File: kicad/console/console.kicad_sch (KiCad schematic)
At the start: 4 parts, among them SW1 SW_DPST_x2

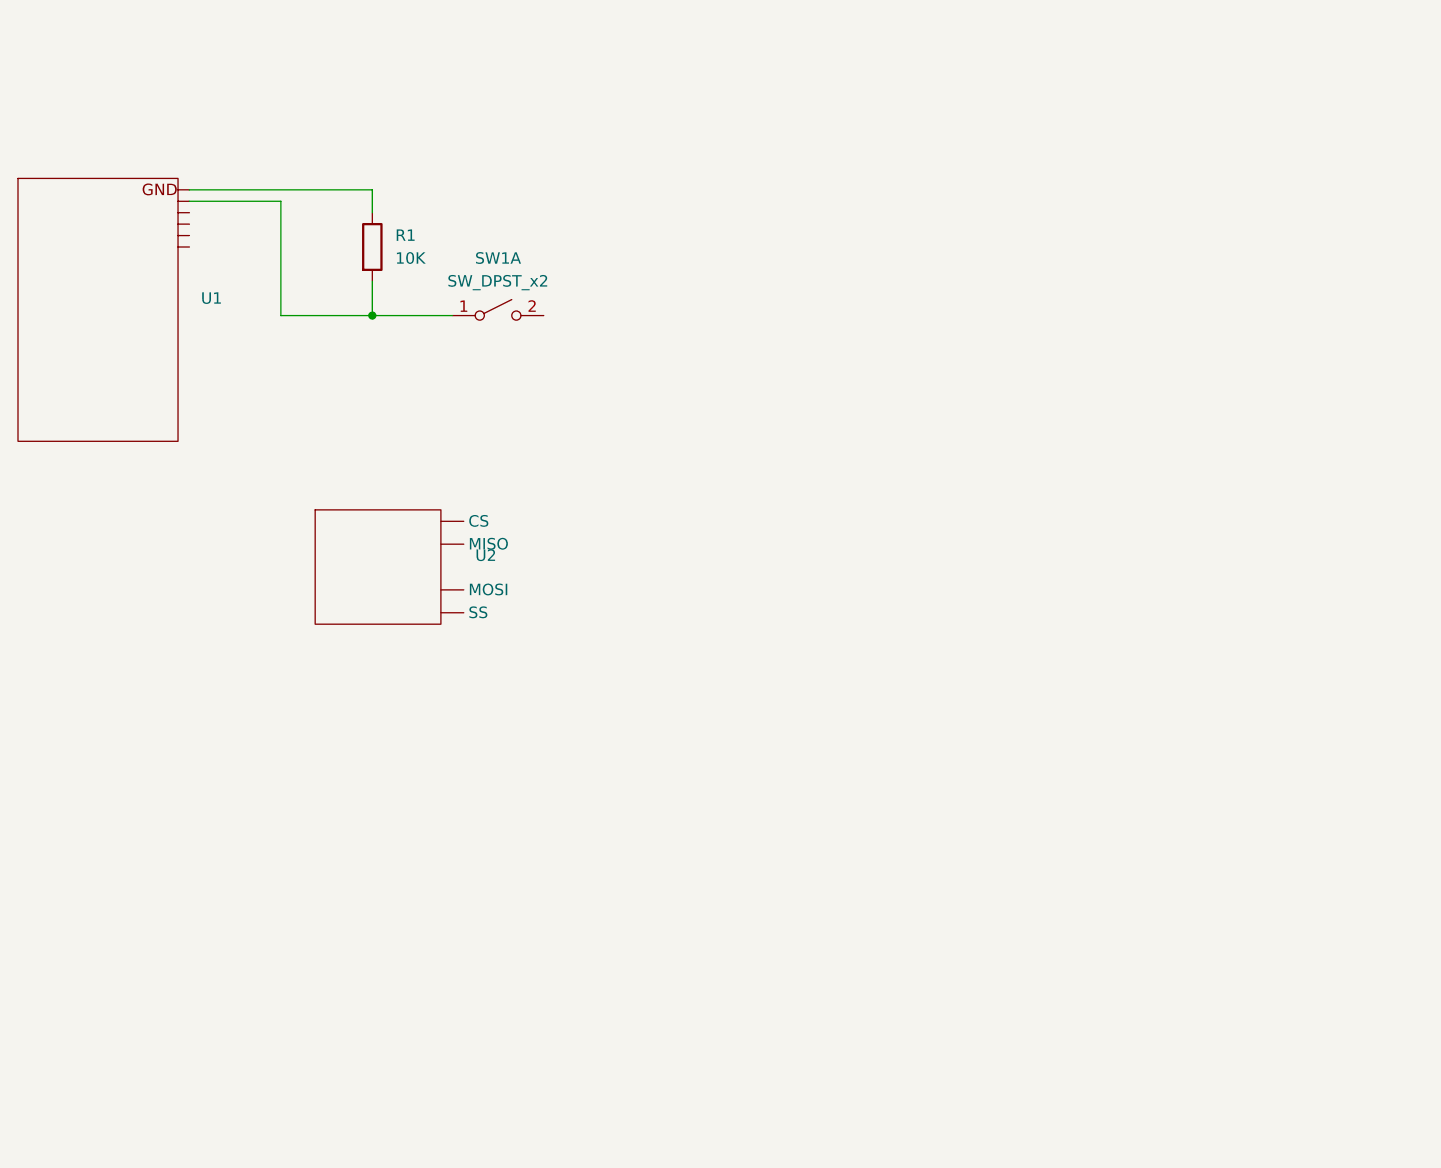
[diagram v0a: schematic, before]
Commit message: kicad schaltplan aktualisiert. es gibt nun eine footprint bibliothek und eine symbolbibliothek.
symbole findet man in der symbols library "console_library" und footprints in der footprint library "console_footprints"
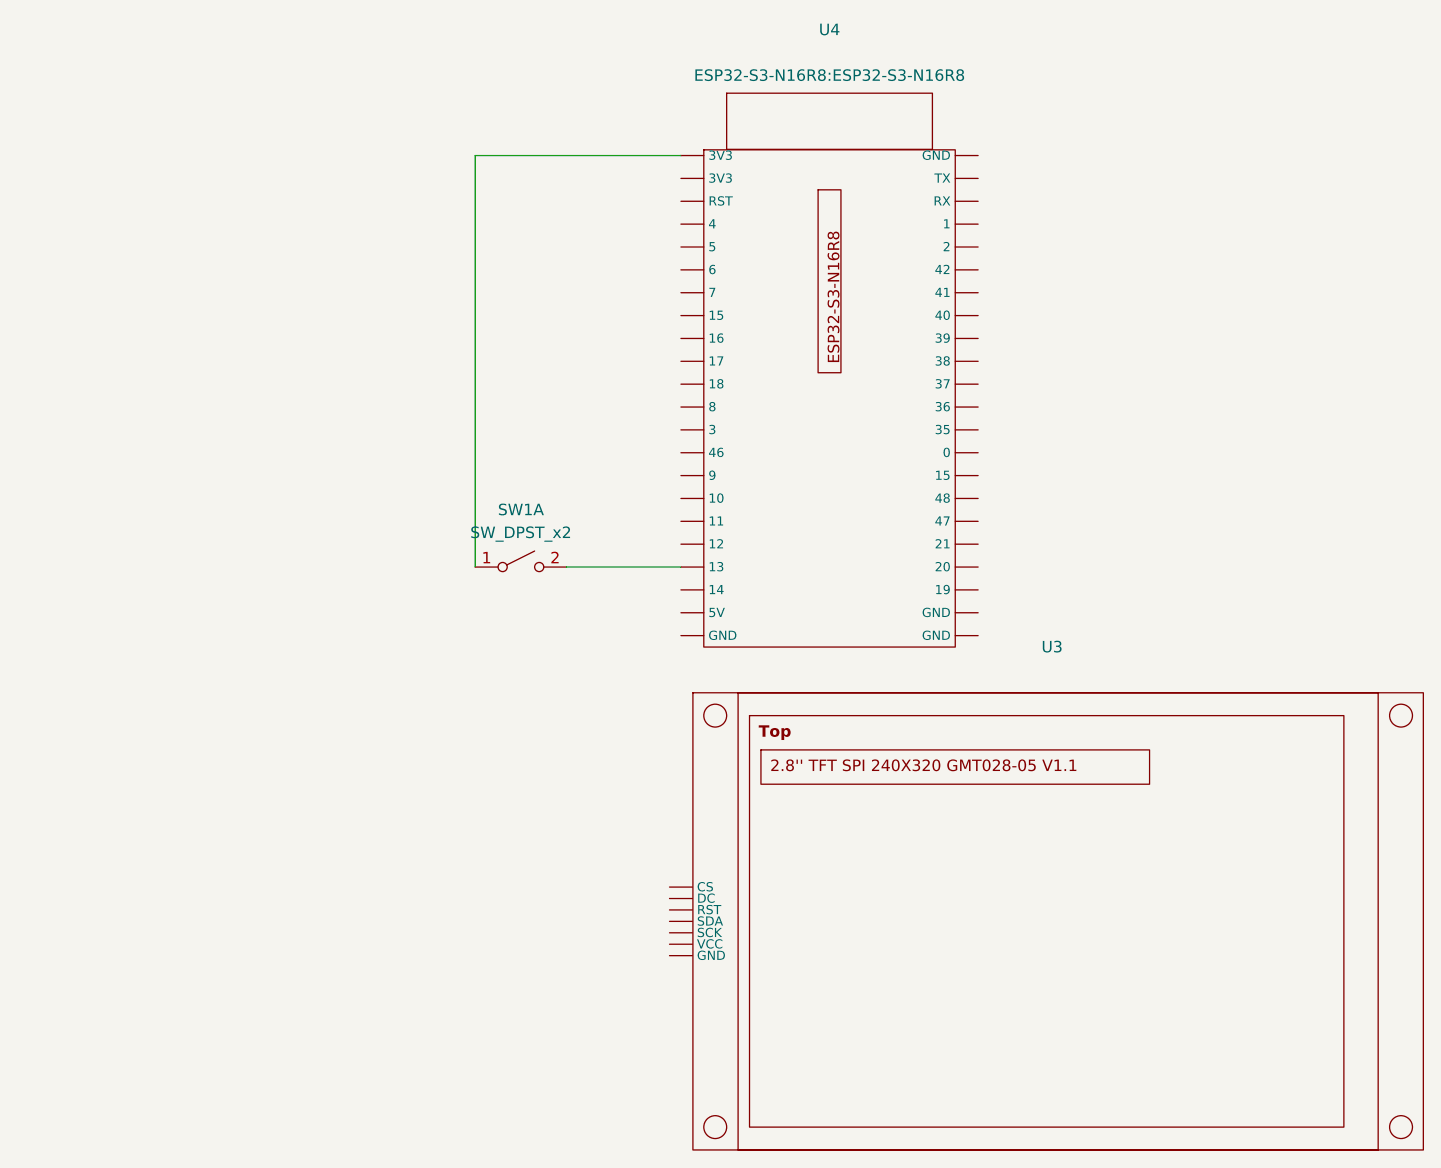
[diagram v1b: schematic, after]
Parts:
- removed R1: 10K, symbol Device:R
- removed U1: ~, symbol console_library:ESP32-S3-N16R8_1
- removed U2: ~, symbol console_library:SPI
- added U3: ~, console_footprints:2.8''_TFT_SPI_240X320_GMT028-05_V1.1, symbol console_library:2.8''_TFT_SPI_240X320_GMT028-05_V1.1
- added U4: ~, ESP32-S3-N16R8:ESP32-S3-N16R8, symbol console_library:ESP32-S3-N16R8
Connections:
- net at SW1.1 (A): now also U4. (GND)
- net at SW1.2 (B): now also U4. (GND)
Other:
- moved on the sheet: SW1A
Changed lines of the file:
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@@
 	(generator_version "9.0")
 	(paper "A4")
-	(junction
-		(at 115.57 68.58)
-		(diameter 0)
-		(color 0 0 0 0)
-	)
 	(wire
 		(pts
-			(xy 115.57 68.58) (xy 124.46 68.58)
+			(xy 137.16 96.52) (xy 149.86 96.52)
 		)
 		(stroke
@@
 	(wire
 		(pts
-			(xy 105.41 55.88) (xy 105.41 68.58)
+			(xy 127 50.8) (xy 149.86 50.8)
 		)
 		(stroke
@@
 	(wire
 		(pts
-			(xy 115.57 57.15) (xy 115.57 54.61)
+			(xy 127 96.52) (xy 127 50.8)
 		)
 		(stroke
@@
 		)
 	)
-	(wire
-		(pts
-			(xy 95.25 54.61) (xy 115.57 54.61)
-		)
-		(stroke
-			(width 0)
-			(type default)
-		)
-	)
-	(wire
-		(pts
-			(xy 115.57 68.58) (xy 105.41 68.58)
-		)
-		(stroke
-			(width 0)
-			(type default)
-		)
-	)
-	(wire
-		(pts
-			(xy 115.57 64.77) (xy 115.57 68.58)
-		)
-		(stroke
-			(width 0)
-			(type default)
-		)
-	)
-	(wire
-		(pts
-			(xy 95.25 55.88) (xy 105.41 55.88)
-		)
-		(stroke
-			(width 0)
-			(type default)
-		)
-	)
 	(symbol
 		(lib_id "Switch:SW_DPST_x2")
-		(at 129.54 68.58 0)
+		(at 132.08 96.52 0)
 		(unit 1)
 		(exclude_from_sim no)
@@
 		(fields_autoplaced yes)
 		(property "Reference" "SW1"
-			(at 129.54 62.23 0)
+			(at 132.08 90.17 0)
 			(effects
 				(font
@@
 		)
 		(property "Value" "SW_DPST_x2"
-			(at 129.54 64.77 0)
+			(at 132.08 92.71 0)
 			(effects
 				(font
@@
 		)
 		(property "Footprint" ""
-			(at 129.54 68.58 0)
+			(at 132.08 96.52 0)
 			(effects
 				(font
@@
 		)
 		(property "Datasheet" "~"
-			(at 129.54 68.58 0)
+			(at 132.08 96.52 0)
 			(effects
 				(font
@@
 		)
 		(property "Description" "Single Pole Single Throw (SPST) switch, separate symbol"
-			(at 129.54 68.58 0)
+			(at 132.08 96.52 0)
 			(effects
 				(font
@@
 	)
 	(symbol
-		(lib_id "Device:R")
-		(at 115.57 60.96 0)
+		(lib_id "console_library:ESP32-S3-N16R8")
+		(at 166.37 78.74 0)
 		(unit 1)
 		(exclude_from_sim no)
@@
 		(dnp no)
 		(fields_autoplaced yes)
-		(property "Reference" "R1"
-			(at 118.11 59.6899 0)
-			(effects
-				(font
-					(size 1.27 1.27)
-				)
-				(justify left)
-			)
-		)
-		(property "Value" "10K"
-			(at 118.11 62.2299 0)
-			(effects
-				(font
-					(size 1.27 1.27)
-				)
-				(justify left)
-			)
-		)
-		(property "Footprint" ""
-			(at 113.792 60.96 90)
-			(effects
-				(font
-					(size 1.27 1.27)
-				)
-				(hide yes)
-			)
-		)
-		(property "Datasheet" "~"
-			(at 115.57 60.96 0)
-			(effects
-				(font
-					(size 1.27 1.27)
-				)
-				(hide yes)
-			)
-		)
-		(property "Description" "Resistor"
-			(at 115.57 60.96 0)
-			(effects
-				(font
-					(size 1.27 1.27)
-				)
-				(hide yes)
-			)
-		)
-		(pin "1"
-		)
-		(pin "2"
+		(property "Reference" "U4"
+			(at 166.37 36.83 0)
+			(effects
+				(font
+					(size 1.27 1.27)
+				)
+			)
+		)
+		(property "Value" "~"
+			(at 166.37 39.37 0)
+			(effects
+				(font
+					(size 1.27 1.27)
+				)
+			)
+		)
+		(property "Footprint" "ESP32-S3-N16R8:ESP32-S3-N16R8"
+			(at 166.37 41.91 0)
+			(effects
+				(font
+					(size 1.27 1.27)
+				)
+			)
+		)
+		(property "Datasheet" ""
+			(at 166.37 78.74 0)
+			(effects
+				(font
+					(size 1.27 1.27)
+				)
+				(hide yes)
+			)
+		)
+		(property "Description" ""
+			(at 166.37 78.74 0)
+			(effects
+				(font
+					(size 1.27 1.27)
+				)
+				(hide yes)
+			)
+		)
+		(pin ""
+		)
+		(pin ""
+		)
+		(pin ""
+		)
+		(pin ""
+		)
+		(pin ""
+		)
+		(pin ""
+		)
+		(pin ""
+		)
+		(pin ""
+		)
+		(pin ""
+		)
+		(pin ""
+		)
+		(pin ""
+		)
+		(pin ""
+		)
+		(pin ""
+		)
+		(pin ""
+		)
+		(pin ""
+		)
+		(pin ""
+		)
+		(pin ""
+		)
+		(pin ""
+		)
+		(pin ""
+		)
+		(pin ""
+		)
+		(pin ""
+		)
+		(pin ""
+		)
+		(pin ""
+		)
+		(pin ""
+		)
+		(pin ""
+		)
+		(pin ""
+		)
+		(pin ""
+		)
+		(pin ""
+		)
+		(pin ""
+		)
+		(pin ""
+		)
+		(pin ""
+		)
+		(pin ""
+		)
+		(pin ""
+		)
+		(pin ""
+		)
+		(pin ""
+		)
+		(pin ""
+		)
+		(pin ""
+		)
+		(pin ""
+		)
+		(pin ""
+		)
+		(pin ""
+		)
+		(pin ""
+		)
+		(pin ""
+		)
+		(pin ""
+		)
+		(pin ""
 		)
 		(instances
 			(project ""
 				(path "/62a2f419-179e-43b6-8483-7e1508ae9f10"
-					(reference "R1")
+					(reference "U4")
 					(unit 1)
 				)
@@
 	)
 	(symbol
-		(lib_id "console_library:SPI")
-		(at 115.57 95.25 0)
+		(lib_id "console_library:2.8''_TFT_SPI_240X320_GMT028-05_V1.1")
+		(at 191.77 135.89 0)
 		(unit 1)
 		(exclude_from_sim no)
@@
 		(dnp no)
 		(fields_autoplaced yes)
-		(property "Reference" "U2"
-			(at 127 95.2499 0)
-			(effects
-				(font
-					(size 1.27 1.27)
-				)
-				(justify left)
+		(property "Reference" "U3"
+			(at 191.1045 105.41 0)
+			(effects
+				(font
+					(size 1.27 1.27)
+				)
 			)
 		)
 		(property "Value" "~"
-			(at 127 97.7899 0)
-			(effects
-				(font
-					(size 1.27 1.27)
-				)
-				(justify left)
-			)
-		)
-		(property "Footprint" ""
-			(at 115.57 95.25 0)
+			(at 191.1045 107.95 0)
+			(effects
+				(font
+					(size 1.27 1.27)
+				)
+			)
+		)
+		(property "Footprint" "console_footprints:2.8''_TFT_SPI_240X320_GMT028-05_V1.1"
+			(at 191.77 135.89 0)
 			(effects
 				(font
@@
 		)
 		(property "Datasheet" ""
-			(at 115.57 95.25 0)
+			(at 191.77 135.89 0)
 			(effects
 				(font
@@
 		)
 		(property "Description" ""
-			(at 115.57 95.25 0)
-			(effects
-				(font
-					(size 1.27 1.27)
-				)
-				(hide yes)
-			)
+			(at 191.77 135.89 0)
+			(effects
+				(font
+					(size 1.27 1.27)
+				)
+				(hide yes)
+			)
+		)
+		(pin ""
+		)
+		(pin ""
+		)
+		(pin ""
 		)
 		(pin ""
@@
 			(project ""
 				(path "/62a2f419-179e-43b6-8483-7e1508ae9f10"
-					(reference "U2")
+					(reference "U3")
 					(unit 1)
 				)
-			)
-		)
-	)
-	(symbol
-		(lib_id "console_library:ESP32-S3-N16R8_1")
-		(at 85.09 69.85 0)
-		(unit 1)
-		(exclude_from_sim no)
-		(in_bom yes)
-		(on_board yes)
-		(dnp no)
-		(fields_autoplaced yes)
-		(property "Reference" "U1"
-			(at 96.52 66.6749 0)
-			(effects
-				(font
-					(size 1.27 1.27)
-				)
-				(justify left)
-			)
-		)
-		(property "Value" "~"
-			(at 96.52 69.2149 0)
-			(effects
-				(font
-					(size 1.27 1.27)
-				)
-				(justify left)
-			)
-		)
-		(property "Footprint" ""
-			(at 85.09 69.85 0)
-			(effects
-				(font
-					(size 1.27 1.27)
-				)
-				(hide yes)
-			)
-		)
-		(property "Datasheet" ""
-			(at 85.09 69.85 0)
-			(effects
-				(font
-					(size 1.27 1.27)
-				)
-				(hide yes)
-			)
-		)
-		(property "Description" ""
-			(at 85.09 69.85 0)
-			(effects
-				(font
-					(size 1.27 1.27)
-				)
-				(hide yes)
-			)
-		)
-		(instances
-			(project ""
-				(path "/62a2f419-179e-43b6-8483-7e1508ae9f10"
-					(reference "U1")
-					(unit 1)
-				)

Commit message: paar connections gezogen
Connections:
- net at U4. (GND): now also U3. (GND)
- new net: U3. (GND), U4. (GND) (x5)
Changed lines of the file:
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@@
+	(wire
+		(pts
+			(xy 148.59 139.7) (xy 134.62 139.7)
+		)
+		(stroke
+			(width 0)
+			(type default)
+		)
+	)
+	(wire
+		(pts
+			(xy 118.11 134.62) (xy 148.59 134.62)
+		)
+		(stroke
+			(width 0)
+			(type default)
+		)
+	)
 	(wire
 		(pts
@@
 	(wire
 		(pts
+			(xy 121.92 73.66) (xy 149.86 73.66)
+		)
+		(stroke
+			(width 0)
+			(type default)
+		)
+	)
+	(wire
+		(pts
+			(xy 134.62 104.14) (xy 149.86 104.14)
+		)
+		(stroke
+			(width 0)
+			(type default)
+		)
+	)
+	(wire
+		(pts
 			(xy 127 96.52) (xy 127 50.8)
 		)
 		(stroke
+			(width 0)
+			(type default)
+		)
+	)
+	(wire
+		(pts
+			(xy 148.59 137.16) (xy 140.97 137.16)
+		)
+		(stroke
+			(width 0)
+			(type default)
+		)
+	)
+	(wire
+		(pts
+			(xy 149.86 76.2) (xy 118.11 76.2)
+		)
+		(stroke
+			(width 0)
+			(type default)
+		)
+	)
+	(wire
+		(pts
+			(xy 134.62 139.7) (xy 134.62 104.14)
+		)
+		(stroke
+			(width 0)
+			(type default)
+		)
+	)
+	(wire
+		(pts
+			(xy 148.59 132.08) (xy 124.46 132.08)
+		)
+		(stroke
+			(width 0)
+			(type default)
+		)
+	)
+	(wire
+		(pts
+			(xy 111.76 53.34) (xy 111.76 138.43)
+		)
+		(stroke
+			(width 0)
+			(type default)
+		)
+	)
+	(wire
+		(pts
+			(xy 140.97 137.16) (xy 140.97 93.98)
+		)
+		(stroke
+			(width 0)
+			(type default)
+		)
+	)
+	(wire
+		(pts
+			(xy 148.59 133.35) (xy 121.92 133.35)
+		)
+		(stroke
+			(width 0)
+			(type default)
+		)
+	)
+	(wire
+		(pts
+			(xy 121.92 133.35) (xy 121.92 73.66)
+		)
+		(stroke
+			(width 0)
+			(type default)
+		)
+	)
+	(wire
+		(pts
+			(xy 124.46 132.08) (xy 124.46 88.9)
+		)
+		(stroke
+			(width 0)
+			(type default)
+		)
+	)
+	(wire
+		(pts
+			(xy 118.11 76.2) (xy 118.11 134.62)
+		)
+		(stroke
+			(width 0)
+			(type default)
+		)
+	)
+	(wire
+		(pts
+			(xy 149.86 53.34) (xy 111.76 53.34)
+		)
+		(stroke
+			(width 0)
+			(type default)
+		)
+	)
+	(wire
+		(pts
+			(xy 140.97 93.98) (xy 149.86 93.98)
+		)
+		(stroke
+			(width 0)
+			(type default)
+		)
+	)
+	(wire
+		(pts
+			(xy 111.76 138.43) (xy 148.59 138.43)
+		)
+		(stroke
+			(width 0)
+			(type default)
+		)
+	)
+	(wire
+		(pts
+			(xy 124.46 88.9) (xy 149.86 88.9)
+		)
+		(stroke
